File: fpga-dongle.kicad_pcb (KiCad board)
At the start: 2 copper layers, 85.8 x 137 mm, 119 parts, among them P1 USB_PWR, P2 PGM, P3 right, P4 left, P5 CONN_01X40, P6 CONN_01X40, P7 DBG_SWD, P8 USB_PWR, Q1 BC857, SW1 T1107A(6x3,8x2,5MM)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

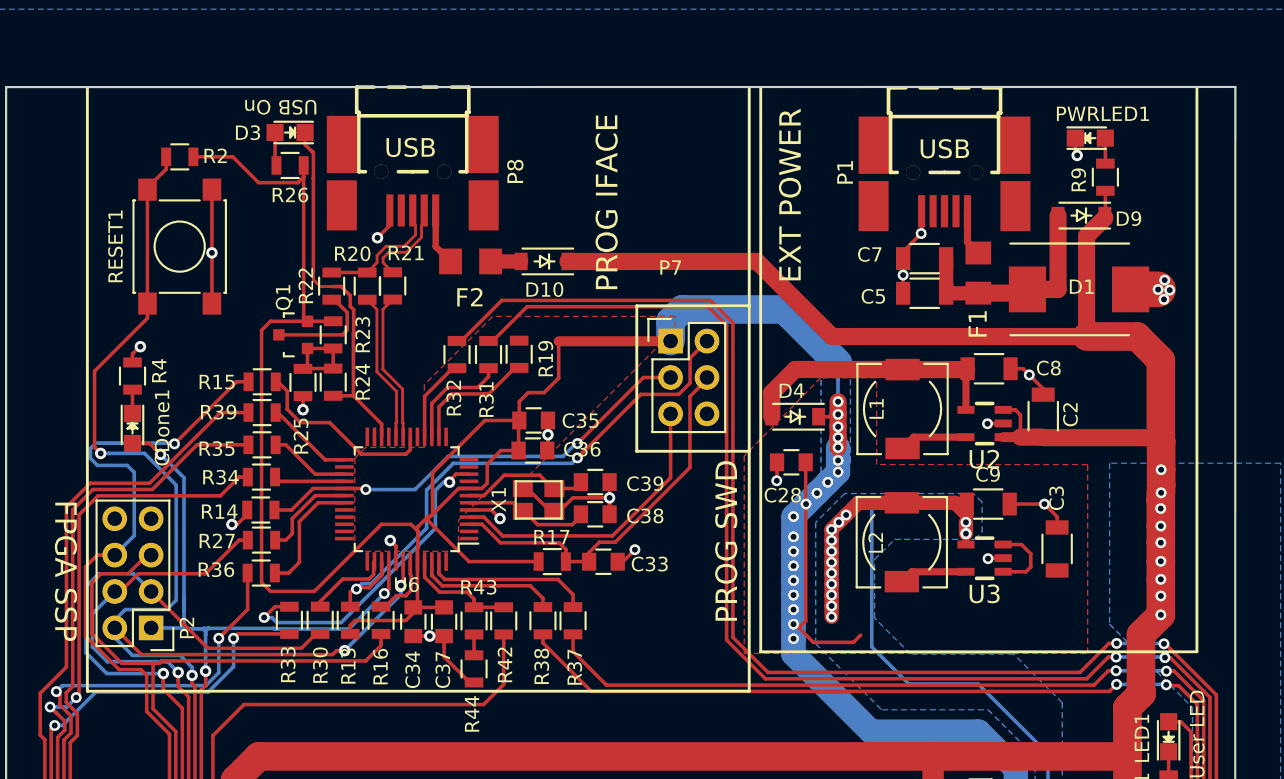
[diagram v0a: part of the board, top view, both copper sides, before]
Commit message: Partial rework of changes lost in last conflict
Signed-off-by: Martin Ribelotta <martinribelotta@gmail.com>
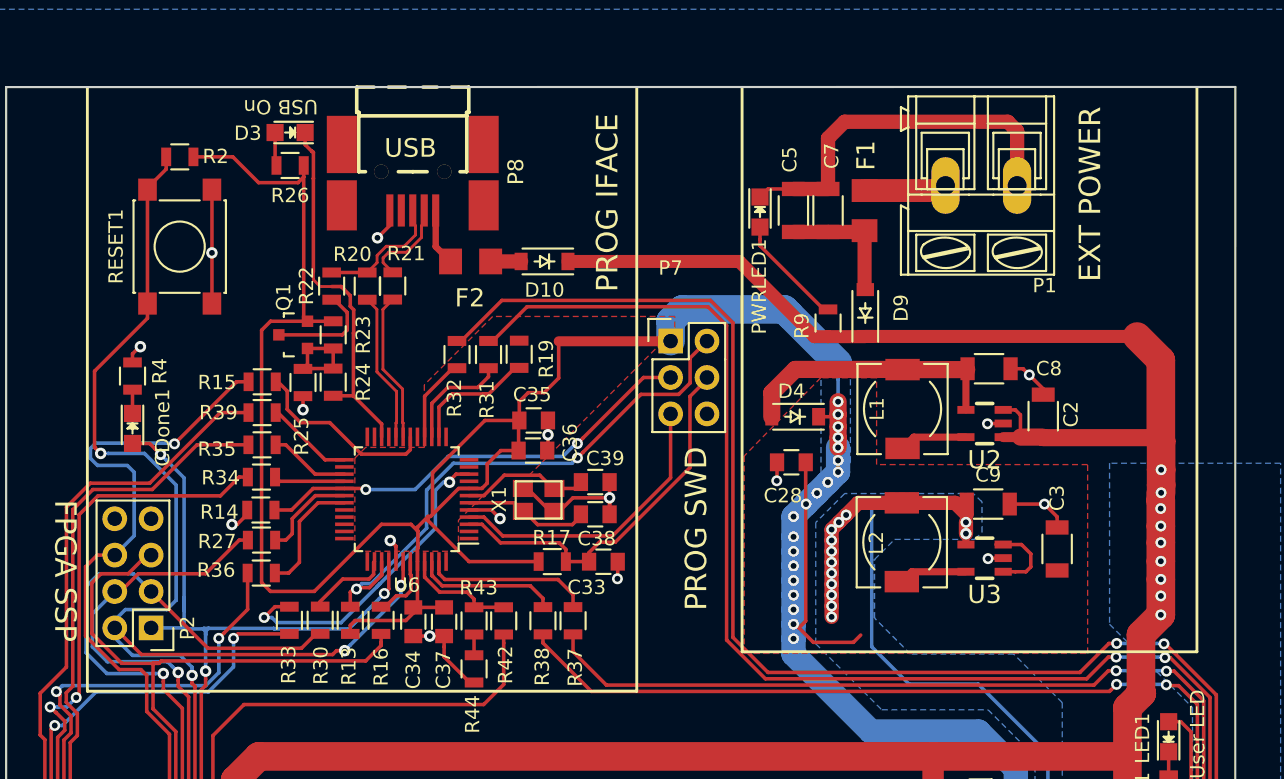
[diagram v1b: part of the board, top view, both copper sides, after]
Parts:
- removed D1: SMBJ6.0A, Diodes_SMD:DO-214AB
- P1: value USB_PWR -> CONN_01X02; footprint OLIMEX_Connectors-FP:USB_Mini-B-NOSILK -> Connect:AK300-2
- moved PWRLED1 23.6 mm to (67.9, 26.4), turned to 270 degrees
- moved R9 21.9 mm to (72.7, 34.1)
- moved D9 16.6 mm to (75.2, 33.4), turned to 90 degrees
- moved C5 10.8 mm to (70.2, 26.2), turned to 270 degrees
- moved F1 9.06 mm to (75.2, 26.2)
- moved C7 7.53 mm to (72.6, 26.2), turned to 270 degrees
- moved P1 5.15 mm to (85.8, 24.5), turned to 180 degrees
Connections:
- P1 pad 1: Net-(F1-Pad1) -> GND
- P1 pad 2: (no net) -> Net-(F1-Pad1)
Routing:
- net GND: track 281.1 -> 294.8 mm, vias 78 -> 71
- net +5V: track 263.0 -> 252.3 mm
- net Net-(C5-Pad2): track 15.5 -> 9.14 mm
- net Net-(PWRLED1-Pad2): track 1.78 -> 7.89 mm
- net Net-(F1-Pad1): track 3.23 -> 6.79 mm

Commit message: More PCB annotations, some rework on GND plane
Signed-off-by: Martin Ribelotta <martinribelotta@gmail.com>
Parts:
- added ?: , OLIMEX_LOGOs-FP:LOGO_OPENHARDWARE_8x8, B.Cu at (36.2, 128.0)
- added ?: , OLIMEX_LOGOs-FP:LOGO_OPENHARDWARE_8x8, F.Cu at (47.2, 128.0)
- added G1: LOGO, mribelotta:LOGO, B.Cu at (48.9, 128.1)
- added G1: LOGO, mribelotta:LOGO, F.Cu at (34.5, 128.1)
- U1: value W25Q16BVSSIG(SOIC-8_208mil) -> W25Q128FVSIG(SOIC-8_208mil)
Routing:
- net /I2C_SDA: track 276.8 -> 283.6 mm
- net /I2C_SCL: track 281.9 -> 288.7 mm
- net /TxD: track 255.8 -> 262.6 mm
- net /RxD: track 253.5 -> 260.2 mm
- net +5V: track 252.3 -> 258.7 mm, vias 14 -> 18
- net GND: track 294.8 -> 300.9 mm
- net /BUT1: track 89.0 -> 93.7 mm
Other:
- board text added: "+"
- board text added: "-"
- board text added: "16MB SPI FLASH"
- board text added: "50MHz OSC"
- board text added: "8-16-32MB SDRAM"
- board text added: "EXPANSION I"
- board text added: "EXPANSION II"
- board text added: "FPGA Dongle iCE40 @ EDU-CIAA-NXP v0.1"
- board text added: "iCE40-HX4K VQ144"

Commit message: Copyright label on board
Signed-off-by: Martin Ribelotta <martinribelotta@gmail.com>
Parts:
- moved R29 1.33 mm to (28.9, 96.5)
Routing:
- net +3V3: track 573.7 -> 599.1 mm, vias 52 -> 57
- net /iCE40-CRESET: track 169.0 -> 163.0 mm, vias 6 -> 5
- net /AUX_SPI_SCK: track 12.8 -> 11.6 mm
- net /iCE40-SCK: track 113.5 -> 112.2 mm
- net /iCE40-CDONE: vias 5 -> 4
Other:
- board text added: "Copyright © 2016 Martin Ribelotta LICENCE Apache 2.0 relic. to CIAA"
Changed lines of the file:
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@@
     (links 420)
     (no_connects 0)
-    (area 15.204999 17.544999 101.155001 154.695001)
+    (area 6.858 12.192 107.696001 163.068001)
     (thickness 1.6)
-    (drawings 54)
-    (tracks 2308)
+    (drawings 55)
+    (tracks 2322)
     (zones 0)
     (modules 122)
@@
   )
   (module Resistors_SMD:R_0805 (layer B.Cu)
-    (at 30.2 96.65 90)
+    (at 28.88 96.49 90)
     (descr "Resistor SMD 0805, reflow soldering, Vishay (see dcrcw.pdf)")
     (tags "resistor 0805")
@@
     (fp_line (start -1.22682 2.46126) (end -0.67564 1.03886) (layer F.SilkS) (width 0.42))
   )
+  (gr_text "Copyright © 2016 Martin Ribelotta\nLICENCE Apache 2.0 relic. to CIAA" (at 43.48 148.06) (layer F.SilkS)
+    (effects (font (size 1.2 1.2) (thickness 0.25)))
+  )
   (gr_line (start 46.25 120.6) (end 46.25 114.82) (layer F.SilkS) (width 0.2))
   (gr_line (start 58.75 120.6) (end 46.25 120.6) (layer F.SilkS) (width 0.2))
@@
     (effects (font (size 1.5 1.5) (thickness 0.3)))
   )
-  (gr_text "FPGA Dongle iCE40 @ EDU-CIAA-NXP v0.1" (at 59.62 150.74) (layer F.SilkS)
-    (effects (font (size 2 2) (thickness 0.3)))
+  (gr_text "FPGA Dongle iCE40 @ EDU-CIAA-NXP v0.1" (at 45.01 151.65) (layer F.SilkS)
+    (effects (font (size 1.2 1.2) (thickness 0.25)))
   )
   (gr_line (start 66.65 17.65) (end 66.65 57.05) (layer F.SilkS) (width 0.2))
-  (gr_text "FPGA SSP" (at 19.4 51.4 270) (layer F.SilkS)
+  (gr_text "FPGA SSP" (at 19.23 51.84 270) (layer F.SilkS)
     (effects (font (size 1.5 1.5) (thickness 0.3)))
   )
@@
   (segment (start 81.802301 103.15) (end 81.743222 103.090921) (width 0.25) (layer B.Cu) (net 0))
   (via (at 81.743222 103.090921) (size 0.8) (drill 0.4) (layers F.Cu B.Cu) (net 0))
+  (segment (start 36.4 95.8) (end 33.9 98.3) (width 1.7) (layer B.Cu) (net 1))
+  (segment (start 38.09 94.11) (end 36.4 95.8) (width 1.7) (layer B.Cu) (net 1))
+  (segment (start 33.9 98.3) (end 33.9 102.164098) (width 1.7) (layer B.Cu) (net 1))
+  (segment (start 33.9 102.164098) (end 33.768266 102.295832) (width 1.7) (layer B.Cu) (net 1))
+  (segment (start 39.37 72.29) (end 39.35 72.31) (width 1.7) (layer B.Cu) (net 1))
+  (segment (start 34.93 73.22) (end 30.3 73.22) (width 1.7) (layer B.Cu) (net 1))
+  (segment (start 30.3 73.22) (end 29.49 72.41) (width 1.7) (layer B.Cu) (net 1))
+  (segment (start 39.35 72.31) (end 35.84 72.31) (width 1.7) (layer B.Cu) (net 1))
+  (segment (start 35.84 72.31) (end 34.93 73.22) (width 1.7) (layer B.Cu) (net 1))
+  (segment (start 29.49 72.41) (end 22.318 72.41) (width 1.7) (layer B.Cu) (net 1))
+  (segment (start 22.318 72.41) (end 22.198 72.29) (width 1.7) (layer B.Cu) (net 1))
+  (segment (start 22.93 63.66) (end 23.77 63.66) (width 1.2) (layer F.Cu) (net 1))
+  (segment (start 22.19 63.66) (end 22.93 63.66) (width 1.2) (layer F.Cu) (net 1))
+  (via (at 22.93 63.66) (size 0.762) (drill 0.4064) (layers F.Cu B.Cu) (net 1))
+  (segment (start 23.77 63.66) (end 24.69 63.66) (width 1.2) (layer F.Cu) (net 1))
+  (via (at 23.77 63.66) (size 0.762) (drill 0.4064) (layers F.Cu B.Cu) (net 1))
+  (segment (start 24.69 63.66) (end 25.66 63.66) (width 1.2) (layer F.Cu) (net 1))
+  (via (at 24.69 63.66) (size 0.762) (drill 0.4064) (layers F.Cu B.Cu) (net 1))
+  (via (at 25.66 63.66) (size 0.762) (drill 0.4064) (layers F.Cu B.Cu) (net 1))
+  (segment (start 22.098 72.39) (end 22.098 63.752) (width 1.2) (layer F.Cu) (net 1))
+  (segment (start 22.098 63.752) (end 22.19 63.66) (width 0.25) (layer F.Cu) (net 1))
+  (via (at 22.19 63.66) (size 0.762) (drill 0.4064) (layers F.Cu B.Cu) (net 1))
+  (segment (start 36.802266 67.499832) (end 36.802266 64.942266) (width 1.7) (layer B.Cu) (net 1))
+  (segment (start 36.802266 64.942266) (end 35.52 63.66) (width 1.7) (layer B.Cu) (net 1))
+  (segment (start 35.52 63.66) (end 22.19 63.66) (width 1.7) (layer B.Cu) (net 1))
   (segment (start 28.35 22.5) (end 31.1 22.5) (width 0.25) (layer F.Cu) (net 1))
   (segment (start 31.1 22.5) (end 32.9 24.3) (width 0.25) (layer F.Cu) (net 1))
@@
   (segment (start 77.732098 72.29) (end 39.37 72.29) (width 1.7) (layer B.Cu) (net 1))
   (segment (start 22.198 72.29) (end 22.098 72.39) (width 0.25) (layer B.Cu) (net 1))
-  (segment (start 39.37 72.29) (end 22.198 72.29) (width 1.7) (layer B.Cu) (net 1))
   (via (at 22.098 72.39) (size 0.762) (drill 0.4064) (layers F.Cu B.Cu) (net 1))
   (segment (start 51.1 40.9) (end 51.1 39.578) (width 0.25) (layer F.Cu) (net 1))
@@
   (segment (start 38.09 72.29) (end 38.09 77.625) (width 1.7) (layer B.Cu) (net 1))
   (segment (start 38.09 77.625) (end 38.09 94.11) (width 1.7) (layer B.Cu) (net 1))
-  (segment (start 38.09 94.11) (end 36.4 95.8) (width 1.7) (layer B.Cu) (net 1))
   (segment (start 61.66 35.36) (end 61.66 33.965) (width 2) (layer B.Cu) (net 1))
   (segment (start 61.66 33.965) (end 62.475 33.15) (width 2) (layer B.Cu) (net 1))
@@
   (segment (start 32 124.58) (end 36.802266 129.382266) (width 1.7) (layer B.Cu) (net 1))
   (segment (start 32 110.238506) (end 32 124.58) (width 1.7) (layer B.Cu) (net 1))
-  (segment (start 36.802266 67.499832) (end 38.08 68.777566) (width 0.25) (layer B.Cu) (net 1))
-  (segment (start 38.08 68.777566) (end 38.08 72.28) (width 0.25) (layer B.Cu) (net 1))
   (segment (start 38.08 72.28) (end 38.09 72.29) (width 0.25) (layer B.Cu) (net 1))
   (segment (start 79.982266 71.537734) (end 79.97 71.55) (width 1.7) (layer B.Cu) (net 1))
@@
   (segment (start 73.35 40.48) (end 73.35 41.34) (width 1.2) (layer F.Cu) (net 1))
   (segment (start 73.35 42.1) (end 73.35 42.79) (width 1.2) (layer F.Cu) (net 1))
-  (segment (start 36.4 95.8) (end 33.9 98.3) (width 1.7) (layer B.Cu) (net 1))
-  (segment (start 33.9 102.164098) (end 33.768266 102.295832) (width 1.7) (layer B.Cu) (net 1))
-  (segment (start 33.9 98.3) (end 33.9 102.164098) (width 1.7) (layer B.Cu) (net 1))
   (segment (start 79.982266 71.537734) (end 79.23 72.29) (width 1.7) (layer B.Cu) (net 1))
   (segment (start 79.23 72.29) (end 77.732098 72.29) (width 1.7) (layer B.Cu) (net 1))
@@
   (segment (start 52.841422 100.90208) (end 52.841422 101.418822) (width 0.25) (layer F.Cu) (net 10))
   (segment (start 53.371751 100.371751) (end 52.841422 100.90208) (width 0.25) (layer F.Cu) (net 10))
-  (segment (start 29.23 102.66) (end 29.22 102.65) (width 0.25) (layer B.Cu) (net 10))
-  (via (at 29.22 102.65) (size 0.762) (drill 0.4064) (layers F.Cu B.Cu) (net 10))
   (segment (start 55.444656 101.2481) (end 54.2481 101.2481) (width 0.25) (layer F.Cu) (net 10))
   (segment (start 54.2481 101.2481) (end 53.371751 100.371751) (width 0.25) (layer F.Cu) (net 10))
@@
   (segment (start 29.85 103.88) (end 29.459178 103.88) (width 0.25) (layer F.Cu) (net 19))
   (via (at 28.75 94.2) (size 0.762) (drill 0.4064) (layers F.Cu B.Cu) (net 19))
-  (segment (start 25.55 107.71) (end 28.982298 104.277702) (width 0.25) (layer B.Cu) (net 19))
   (segment (start 21.450001 37.457999) (end 21.450001 42.770001) (width 0.25) (layer F.Cu) (net 19))
   (segment (start 25.144 33.764) (end 21.450001 37.457999) (width 0.25) (layer F.Cu) (net 19))
@@
   (segment (start 21.450001 42.770001) (end 21.480001 42.800001) (width 0.25) (layer F.Cu) (net 19))
   (via (at 21.88 43.2) (size 0.8) (drill 0.4) (layers F.Cu B.Cu) (net 19))
-  (segment (start 28.982298 104.277702) (end 29.545511 104.277702) (width 0.25) (layer B.Cu) (net 19))
-  (segment (start 29.545511 104.277702) (end 29.92651 103.896703) (width 0.25) (layer B.Cu) (net 19))
   (segment (start 29.85 103.88) (end 29.909807 103.88) (width 0.25) (layer F.Cu) (net 19))
-  (via (at 29.92651 103.896703) (size 0.762) (drill 0.4064) (layers F.Cu B.Cu) (net 19))
   (segment (start 29.909807 103.88) (end 29.92651 103.896703) (width 0.25) (layer F.Cu) (net 19))
   (segment (start 31.3 103.88) (end 29.85 103.88) (width 0.25) (layer F.Cu) (net 19))
@@
   (segment (start 29.203571 51.6) (end 31.553571 49.25) (width 0.25) (layer F.Cu) (net 21))
   (segment (start 31.553571 49.25) (end 32.153571 49.25) (width 0.25) (layer F.Cu) (net 21) (status 20))
+  (segment (start 28.88 95.54) (end 27.663958 95.54) (width 0.25) (layer B.Cu) (net 22))
+  (segment (start 27.663958 95.54) (end 27.303958 95.9) (width 0.25) (layer B.Cu) (net 22))
   (segment (start 25.95 57.85) (end 26.116638 57.683362) (width 0.25) (layer F.Cu) (net 22))
   (segment (start 40.37558 57.683362) (end 41.45 56.608942) (width 0.25) (layer F.Cu) (net 22))
@@
   (segment (start 27.122477 62.618255) (end 25.531447 61.027225) (width 0.25) (layer F.Cu) (net 22))
   (segment (start 25.531447 61.027225) (end 25.531447 57.85) (width 0.25) (layer F.Cu) (net 22))
-  (segment (start 30.2 95.7) (end 30.02 95.88) (width 0.25) (layer B.Cu) (net 22))
-  (segment (start 30.02 95.88) (end 27.323958 95.88) (width 0.25) (layer B.Cu) (net 22))
   (segment (start 27.323958 95.88) (end 27.303958 95.9) (width 0.25) (layer B.Cu) (net 22))
   (segment (start 48.36826 105.52499) (end 47.818249 106.075001) (width 0.25) (layer F.Cu) (net 22))
@@
   (segment (start 24.65 86.08) (end 26.475 87.905) (width 0.25) (layer B.Cu) (net 156))
   (segment (start 27.922976 91.45) (end 28.05 91.45) (width 0.25) (layer B.Cu) (net 156))
-  (segment (start 30.2 97.6) (end 26.9 97.6) (width 0.25) (layer B.Cu) (net 157))
+  (segment (start 28.88 97.44) (end 27.98 97.44) (width 0.25) (layer B.Cu) (net 157))
+  (segment (start 27.98 97.44) (end 27.82 97.6) (width 0.25) (layer B.Cu) (net 157))
+  (segment (start 27.82 97.6) (end 26.9 97.6) (width 0.25) (layer B.Cu) (net 157))
   (segment (start 26.9 97.6) (end 25.985458 96.685458) (width 0.25) (layer B.Cu) (net 157))
   (segment (start 25.985458 96.685458) (end 25.985458 95.470244) (width 0.25) (layer B.Cu) (net 157))
